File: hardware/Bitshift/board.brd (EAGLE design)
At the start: 101.6 x 101.6 mm, 16 parts, among them Q1 MOSFET-NCHANNELFDS6630A, U1 Tiny85-20-SMT

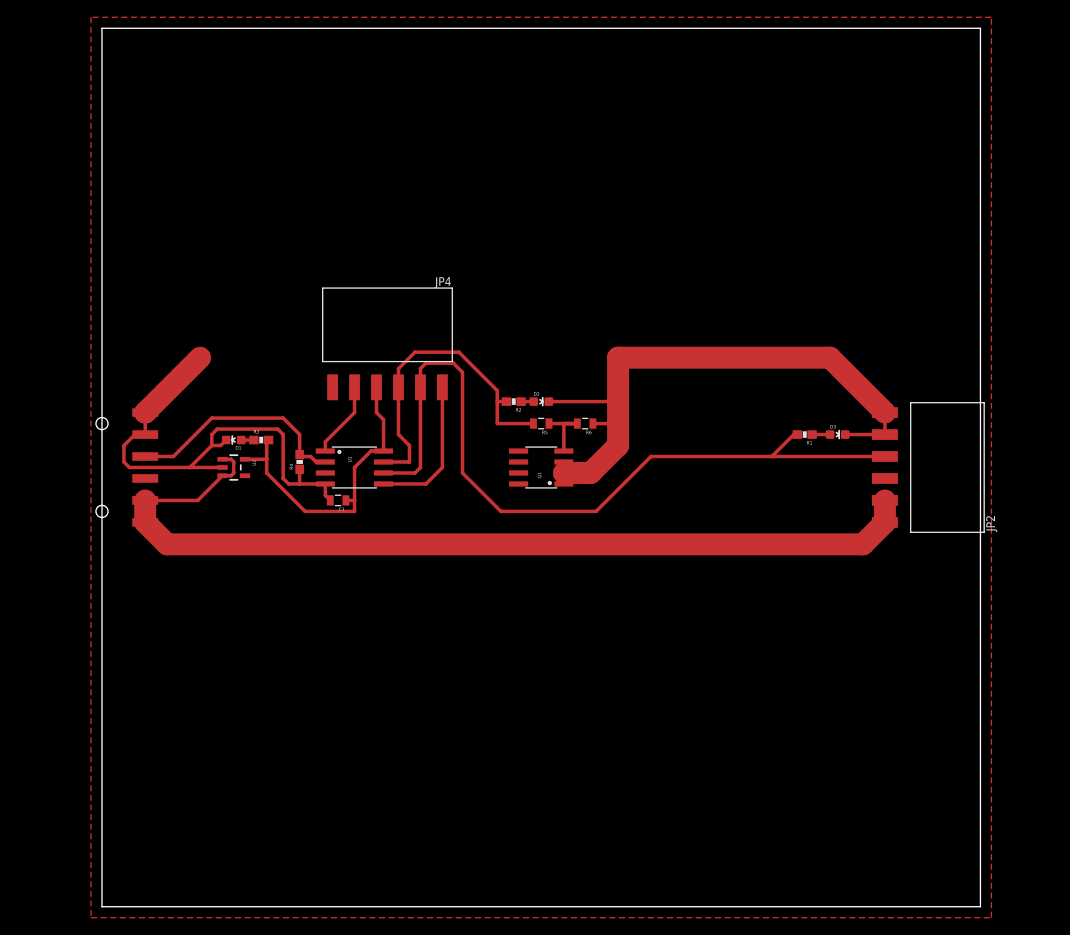
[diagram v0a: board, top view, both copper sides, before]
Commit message: added decoupling cap for voltage regulator in BOM
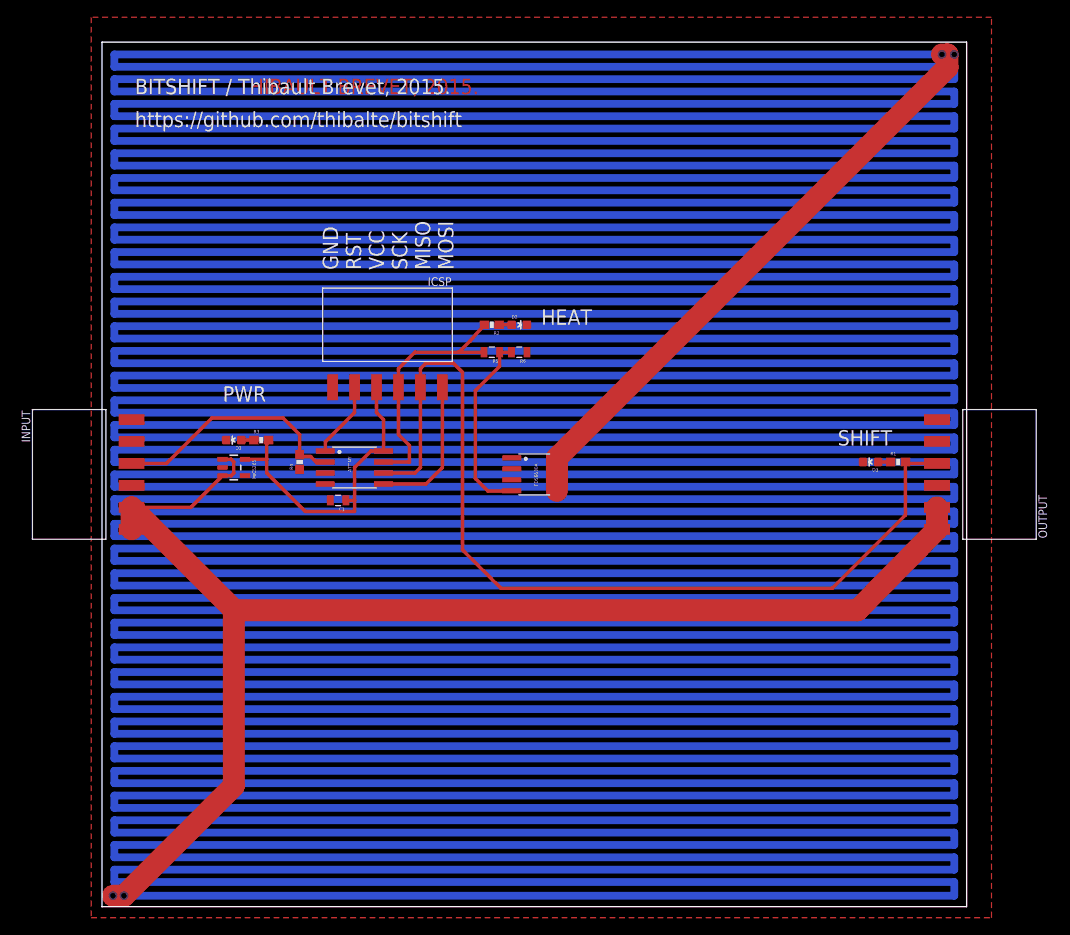
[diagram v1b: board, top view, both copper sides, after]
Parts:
- removed JP1: RA 6Pin SMD, SparkFun-Connectors:1X06-SMD
- removed JP2: (no value), SparkFun-Connectors:1X06-SMD-FEMALE-V2
- removed Q1: MOSFET-NCHANNELFDS6630A, SparkFun-DiscreteSemi:SO08
- added FDS6630A: MOSFET-NCHANNELFDS6630A, SparkFun-DiscreteSemi:SO08
- added INPUT, OUTPUT: (no value), SparkFun-Connectors:1X06-SMD-FEMALE-V2
- C1: value 1.0uF -> 0.1uF
- R1, R2, R3: value (none) -> 330
- R4, R5: value (none) -> 10k
- R6: value (none) -> 1M
- moved R1 11.3 mm to (92.1, 51.4), turned to 0 degrees
- moved R6 11.2 mm to (48.3, 64.1)
- moved R5 10.0 mm to (45.1, 64.1)
- moved D2 9.25 mm to (48.3, 67.3)
- moved R2 9.25 mm to (45.1, 67.3)
- moved D3 4.96 mm to (88.9, 51.4), turned to 90 degrees
- renumbered JP4 to ICSP, U1 to ATTINY, U2 to MIC5205
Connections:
- net GND: now also FDS6630A.1, FDS6630A.2, FDS6630A.3, INPUT.5, INPUT.6, OUTPUT.1, OUTPUT.2; no longer JP1.1, JP1.2, JP2.1, JP2.2, Q1.1, Q1.2, Q1.3
- net N$5: now also INPUT.4; no longer JP1.3
- net N$6: now also OUTPUT.3; no longer JP2.3
- net N$8: now also FDS6630A.4; no longer Q1.4
- net VCC: now also FDS6630A.5, FDS6630A.6, FDS6630A.7, FDS6630A.8, INPUT.1, INPUT.2, OUTPUT.5, OUTPUT.6; no longer JP1.5, JP1.6, JP2.5, JP2.6, Q1.5, Q1.6, Q1.7, Q1.8
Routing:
- net VCC: track 107.1 -> 7033.2 mm, vias 0 -> 4
- net GND: track 129.6 -> 0.00 mm
- net N$6: track 90.5 -> 108.5 mm
- net N$8: track 8.02 -> 21.9 mm
- net N$9: track 37.4 -> 29.3 mm
- net N$5: track 26.2 -> 28.0 mm
- net N$3: track 2.08 -> 1.45 mm
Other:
- board size 101.6 x 101.6 mm -> 100 x 100 mm
- board text added: "BITSHIFT / THIBAULT BREVET, 2015."
- board text added: "BITSHIFT / Thibault Brevet, 2015."
- board text added: "GND RST VCC SCK MISO MOSI"
- board text added: "HEAT"
- board text added: "PWR"
- board text added: "SHIFT"
- board text added: "https://github.com/thibalte/bitshift"

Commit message: moved things around
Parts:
- added C2: 0.1uF, SparkFun-Capacitors:0805
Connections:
- net GND: now also C2.2
- net N$4: now also C2.1
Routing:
- net N$4: track 36.3 -> 39.3 mm
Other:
- board text removed: "BITSHIFT / THIBAULT BREVET, 2015."
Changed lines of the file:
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@@
 <layer number="14" name="Route14" color="1" fill="6" visible="no" active="no"/>
 <layer number="15" name="Route15" color="4" fill="6" visible="no" active="no"/>
-<layer number="16" name="Bottom" color="1" fill="1" visible="yes" active="yes"/>
+<layer number="16" name="Bottom" color="1" fill="1" visible="no" active="yes"/>
 <layer number="17" name="Pads" color="2" fill="1" visible="no" active="yes"/>
 <layer number="18" name="Vias" color="2" fill="1" visible="yes" active="yes"/>
-<layer number="19" name="Unrouted" color="6" fill="1" visible="no" active="yes"/>
+<layer number="19" name="Unrouted" color="6" fill="1" visible="yes" active="yes"/>
 <layer number="20" name="Dimension" color="15" fill="1" visible="yes" active="yes"/>
 <layer number="21" name="tPlace" color="7" fill="1" visible="yes" active="yes"/>
-<layer number="22" name="bPlace" color="7" fill="1" visible="no" active="yes"/>
+<layer number="22" name="bPlace" color="7" fill="1" visible="yes" active="yes"/>
 <layer number="23" name="tOrigins" color="15" fill="1" visible="yes" active="yes"/>
-<layer number="24" name="bOrigins" color="15" fill="1" visible="no" active="yes"/>
+<layer number="24" name="bOrigins" color="15" fill="1" visible="yes" active="yes"/>
 <layer number="25" name="tNames" color="7" fill="1" visible="yes" active="yes"/>
-<layer number="26" name="bNames" color="7" fill="1" visible="no" active="yes"/>
+<layer number="26" name="bNames" color="7" fill="1" visible="yes" active="yes"/>
 <layer number="27" name="tValues" color="7" fill="1" visible="no" active="yes"/>
 <layer number="28" name="bValues" color="7" fill="1" visible="no" active="yes"/>
@@
 <layer number="42" name="bRestrict" color="1" fill="10" visible="no" active="yes"/>
 <layer number="43" name="vRestrict" color="2" fill="10" visible="no" active="yes"/>
-<layer number="44" name="Drills" color="7" fill="1" visible="no" active="yes"/>
+<layer number="44" name="Drills" color="7" fill="1" visible="yes" active="yes"/>
 <layer number="45" name="Holes" color="7" fill="1" visible="no" active="yes"/>
 <layer number="46" name="Milling" color="3" fill="1" visible="no" active="yes"/>
@@
 <wire x1="100" y1="100" x2="0" y2="100" width="0" layer="20"/>
 <wire x1="0" y1="100" x2="0" y2="0" width="0" layer="20"/>
-<text x="3.81" y="93.98" size="1.778" layer="1">BITSHIFT / THIBAULT BREVET, 2015.</text>
 <text x="40.64" y="73.66" size="1.778" layer="25" font="vector" rot="R90">GND
 RST
@@
 <text x="13.97" y="58.42" size="1.778" layer="25" font="vector">PWR</text>
 <text x="85.09" y="53.34" size="1.778" layer="25" font="vector">SHIFT</text>
-<text x="3.81" y="93.98" size="1.778" layer="25" font="vector">BITSHIFT / Thibault Brevet, 2015.</text>
-<text x="3.81" y="90.17" size="1.778" layer="25" font="vector">https://github.com/thibalte/bitshift</text>
+<text x="3.81" y="95.25" size="1.778" layer="25" font="vector">BITSHIFT / Thibault Brevet, 2015.</text>
+<text x="3.81" y="91.44" size="1.778" layer="25" font="vector">https://github.com/thibalte/bitshift</text>
 </plain>
 <attributes>
@@
 <element name="ICSP" library="SparkFun-Connectors" package="1X06-SMD-FEMALE-V2" value="" x="33.02" y="63.5" rot="R180"/>
 <element name="INPUT" library="SparkFun-Connectors" package="1X06-SMD-FEMALE-V2" value="" x="0" y="50" rot="R270"/>
+<element name="C2" library="SparkFun-Capacitors" package="0805" value="0.1uF" x="17.145" y="47.625" rot="R180">
+<attribute name="PROD_ID" value="CAP-11625" x="17.145" y="47.625" size="1.778" layer="27" font="vector" rot="R180" display="off"/>
+</element>
 </elements>
 <signals>
@@
 <contactref element="INPUT" pad="6"/>
 <contactref element="INPUT" pad="5"/>
+<contactref element="C2" pad="2"/>
 </signal>
 <signal name="VCC">
@@
 <contactref element="ICSP" pad="3"/>
 <wire x1="31.75" y1="57.15" x2="31.75" y2="60.075" width="0.4064" layer="1"/>
+<contactref element="C2" pad="1"/>
+<wire x1="18.045" y1="47.625" x2="19.05" y2="48.63" width="0.4064" layer="1"/>
+<wire x1="19.05" y1="48.63" x2="19.05" y2="50.165" width="0.4064" layer="1"/>
 </signal>
 <signal name="N$5">
